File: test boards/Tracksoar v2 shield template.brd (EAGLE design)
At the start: 44.2 x 19.6 mm, 3 parts

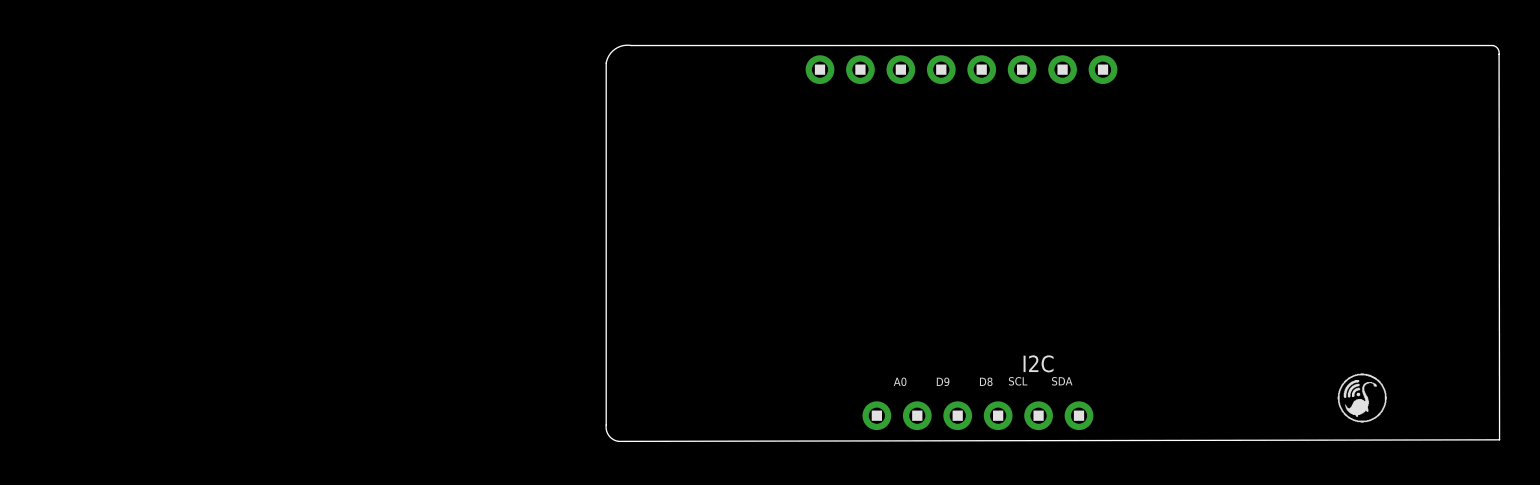
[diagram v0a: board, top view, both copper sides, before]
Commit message: updated shield template
updated shield template to be a breakout board for all IO into .1" headers
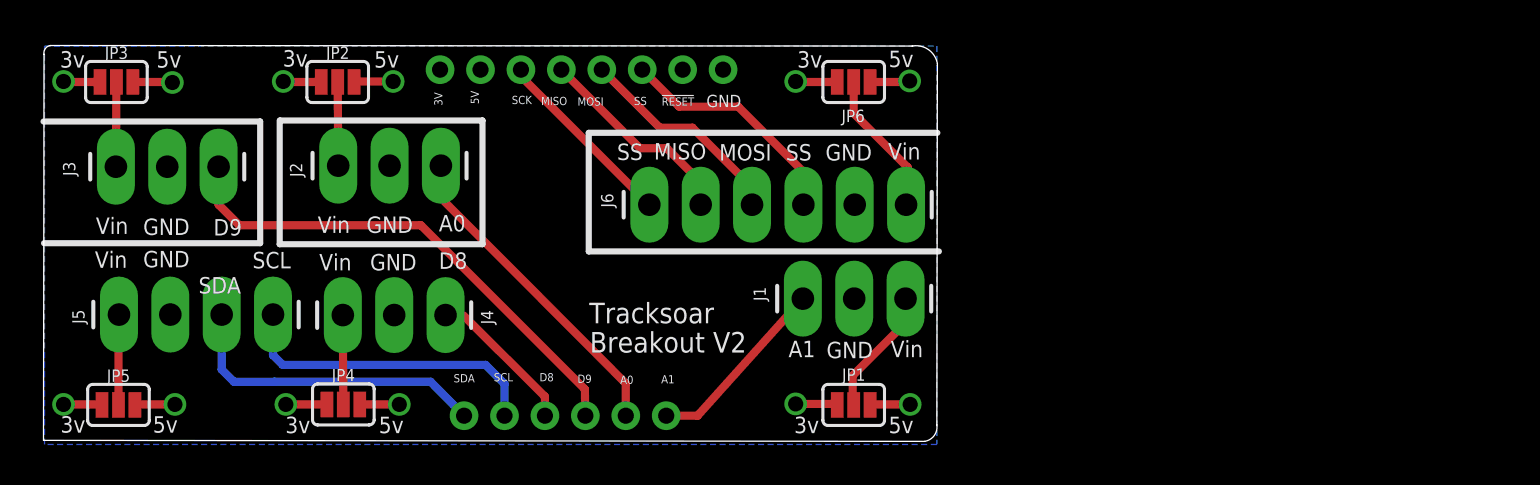
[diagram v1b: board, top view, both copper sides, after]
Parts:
- added J1, J2, J3, J4: (no value), SparkFun-Connectors:1X03_LONGPADS
- added J5: (no value), SparkFun-Connectors:1X04_LONGPADS
- added J6: (no value), SparkFun-Connectors:1X06_LONGPADS
- added JP1, JP2, JP3, JP4, JP5, JP6: JUMPER-SMT_3_1-NC_PASTE_SILK, SparkFun-Jumpers:SMT-JUMPER_3_1-NC_PASTE_SILK
- moved U$3 20.4 mm to (-2.01, 1.24), flipped to the bottom
- moved FTDI 18.8 mm to (-1.19, 18.4), flipped to the bottom
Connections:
- new net N$1: J1.1, JP1.2
- new net N$2: J2.1, JP2.2
- new net N$3: J3.1, JP3.2
- new net N$6: J4.1, JP4.2
- new net N$7: J5.1, JP5.2
- new net N$8: J6.1, JP6.2
- net 3V: now also JP1.1, JP2.1, JP3.1, JP4.1, JP5.1, JP6.1
- net A0: now also J2.3
- net A1: now also J1.3
- net D8: now also J4.3
- net D9: now also J3.3
- net GND: now also J1.2, J2.2, J3.2, J4.2, J5.2, J6.2
- net MISO: now also J6.5
- net MOSI: now also J6.4
- net SCK: now also J6.6
- net SCL: now also J5.4
- net SDA: now also J5.3
- net SS: now also J6.3
- net VCC: now also JP1.3, JP2.3, JP3.3, JP4.3, JP5.3, JP6.3
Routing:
- net D9: track 0.00 -> 25.1 mm
- net A0: track 0.00 -> 16.2 mm
- net SDA: track 0.00 -> 15.7 mm
- net SCL: track 0.00 -> 15.6 mm
- net VCC: track 0.00 -> 11.8 mm, vias 0 -> 6
- net 3V: track 0.00 -> 11.8 mm, vias 0 -> 6
- net SS: track 0.00 -> 11.7 mm
- net MOSI: track 0.00 -> 10.8 mm
- net MISO: track 0.00 -> 10.3 mm
- net A1: track 0.00 -> 9.34 mm
- net SCK: track 0.00 -> 9.31 mm
- net D8: track 0.00 -> 7.52 mm
- net N$8: track 0.00 -> 7.21 mm
- net N$1: track 0.00 -> 6.37 mm
- net N$7: track 0.00 -> 4.47 mm
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- added copper zone on layer 16, net 3V
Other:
- outline, holes or cut-outs redrawn
- board text added: "3v"
- board text added: "5v"
- board text added: "A1"
- board text added: "Breakout V2"
- board text added: "Tracksoar"
- board text added: "Vin"
- board text removed: "I2C"
- board text removed: "SPI"

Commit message: fixed short on serial RX of tracksoar v2
fixed a short on the serial rx line that shorted it to ground due to a via. Updated silkscreen on the breakout board and named headers
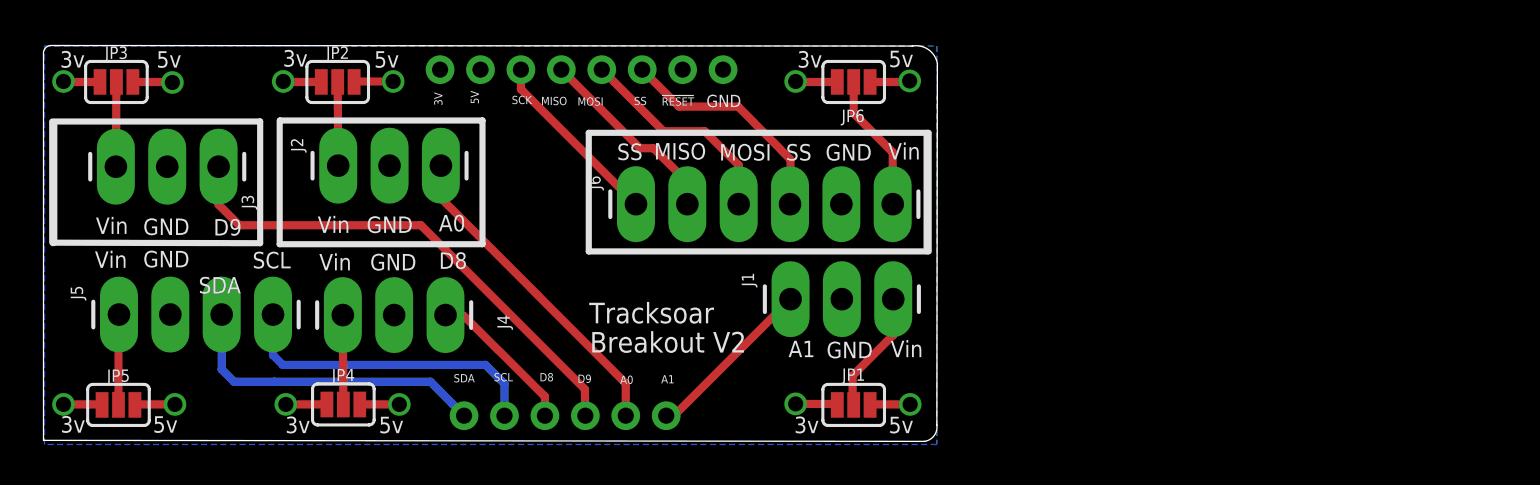
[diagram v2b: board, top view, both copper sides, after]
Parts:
- J1: value (none) -> Analog 1
- J2: value (none) -> Analog 0
- J3: value (none) -> Digital IO 9
- J4: value (none) -> Digital IO 8
- J5: value (none) -> I2C
- J6: value (none) -> SPI
- moved J6 0.66 mm to (14.2, 11.7)
- moved J1 0.61 mm to (14.2, 7.01)
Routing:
- net A1: track 9.34 -> 8.54 mm
- net MISO: track 10.3 -> 9.63 mm
